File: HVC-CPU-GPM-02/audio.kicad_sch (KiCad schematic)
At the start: 0 parts

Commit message: Refactor schematic: * Move audio and video circuits to dedicated sheet * Move power and mechanical to dedicated sheet Modify P1 Cart Connector symbol to: * split out audio ports * organize pins for easier wiring Modify 74LS346 symbol: * Split A/B ports to allow moving functions to related circuits Modify X1 crystal footprint: * change from stock footprint to custom footprint Correct crystal name from Y1 to X1
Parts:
- added C34: 330p, Nintendo:C_Disc_D3.0mm_W2.0mm_P3.0mm, symbol Device:C
- added C35: 0.01u, Nintendo:C_Disc_D3.0mm_W2.0mm_P3.0mm, symbol Device:C
- added C7: 1u, Capacitor_THT:CP_Radial_D5.0mm_P2.50mm, symbol Device:C_Polarized
- added FC1: 39u, Inductor_THT:L_Axial_L5.0mm_D3.6mm_P10.00mm_Horizontal_Murata_BL01RN1A2A2, symbol Device:L_Ferrite
- added FC2: FerriteBead, Inductor_THT:L_Axial_L5.0mm_D3.6mm_P10.00mm_Horizontal_Murata_BL01RN1A2A2, symbol Device:FerriteBead
- added P1: CARTRIGE SLOT, Nintendo:Famicom_2x30_cartridge_connector, symbol Famicom:60p_cart_connector
- added Q1: 2SA937, Nintendo:PACKAGE_TRANSISTOR_FTR, symbol Simulation_SPICE:PNP
- added R1, R2: 100, Resistor_THT:R_Axial_DIN0207_L6.3mm_D2.5mm_P10.16mm_Horizontal, symbol Device:R
- added R3: 10k, Resistor_THT:R_Axial_DIN0207_L6.3mm_D2.5mm_P10.16mm_Horizontal, symbol Device:R
- added R4: 20k, Resistor_THT:R_Axial_DIN0207_L6.3mm_D2.5mm_P10.16mm_Horizontal, symbol Device:R
- added R5: 12, Resistor_THT:R_Axial_DIN0207_L6.3mm_D2.5mm_P10.16mm_Horizontal, symbol Device:R
- added R6: 150, Resistor_THT:R_Axial_DIN0207_L6.3mm_D2.5mm_P10.16mm_Horizontal, symbol Device:R
- added R7: 43k, Resistor_THT:R_Axial_DIN0207_L6.3mm_D2.5mm_P10.16mm_Horizontal, symbol Device:R
- added U7: 74LS368, Package_DIP:DIP-16_W7.62mm, symbol Famicom:74LS368
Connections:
- new net: C7.2, R3.2, R4.2, R5.2
- new net +5V: R6.1
- new net AUX_SND: C7.1, R7.1, U7.14 (IN2b)
- new net CPU_SND1: R2.1, R4.1
- new net CPU_SND2: R1.1, R5.1
- new net GND: C34.2, C35.2, Q1.1 (C), R1.2, R2.2, U7.15 (~{OEb})
- new net MIC: R3.1
- new net PA13: U7.12 (IN1b)
- new net PPU_VIDEO: Q1.2 (B)
- new net RF_AUDIO: C35.1, FC1.2
- new net RF_VIDEO: C34.1, FC2.2
- new net SOUND: P1.45 (SNDI), R7.2, U7.13 (~{OUT2b})
- new net SOUND+CART: FC1.1, P1.46 (SNDO)
- new net VID_A: FC2.1, Q1.3 (E), R6.2
- new net ~{PA13}: U7.11 (~{OUT1b})
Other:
- note added: "AUDIO MIXER"
- note added: "VIDEO AMP"

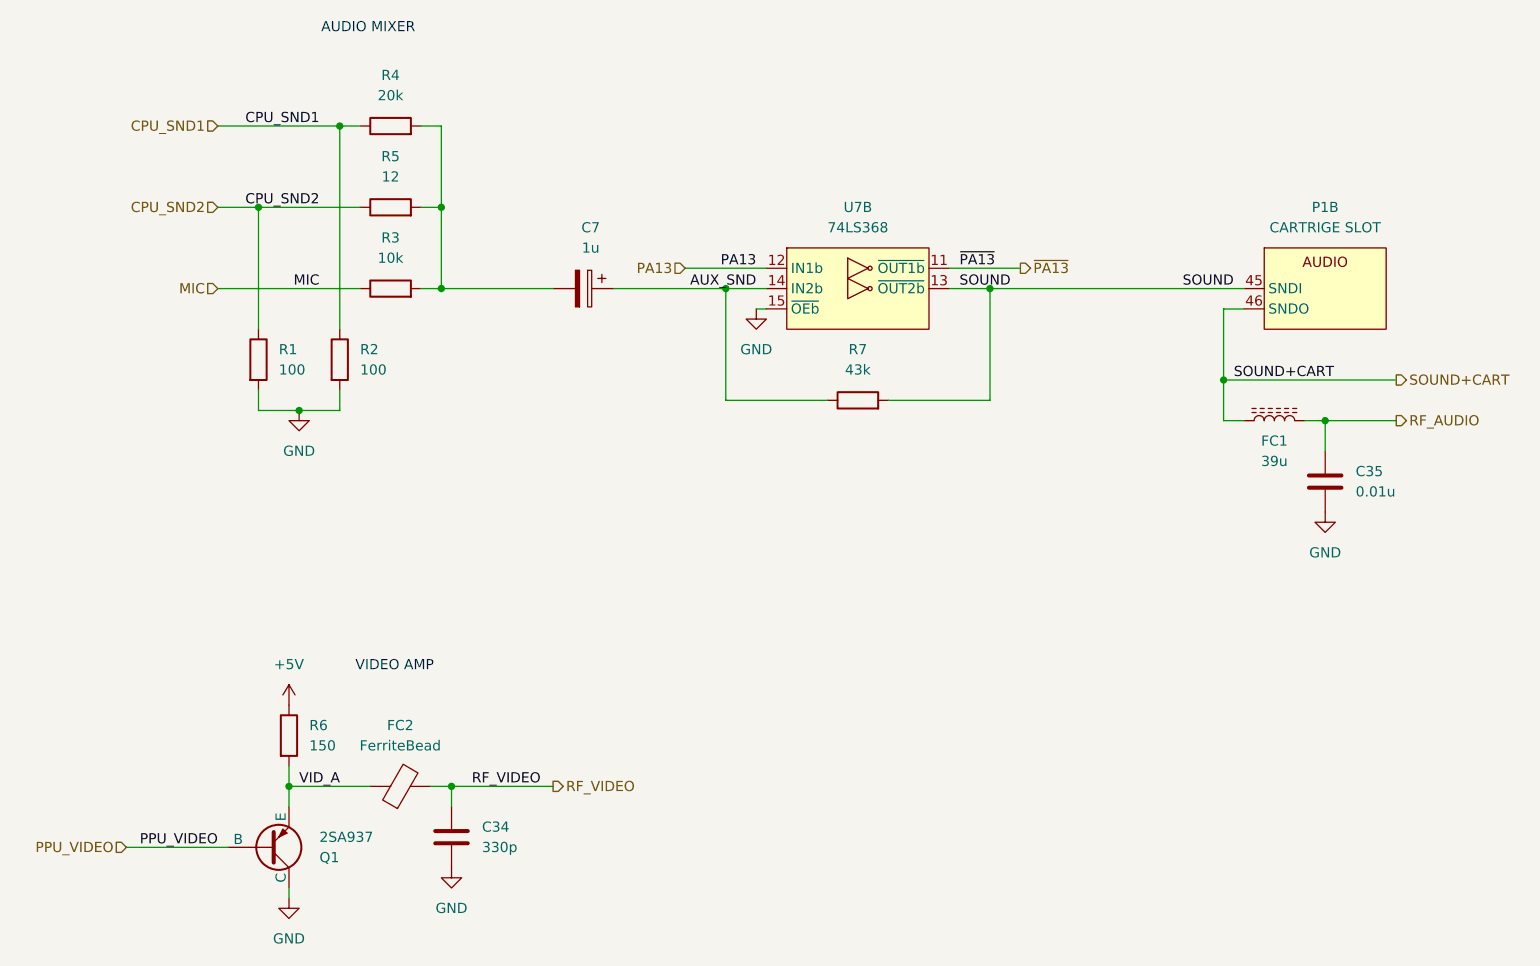
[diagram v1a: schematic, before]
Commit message: Change symbols to functional layout instead of pin map layout Add technical page to store pinouts Organize and compact root page
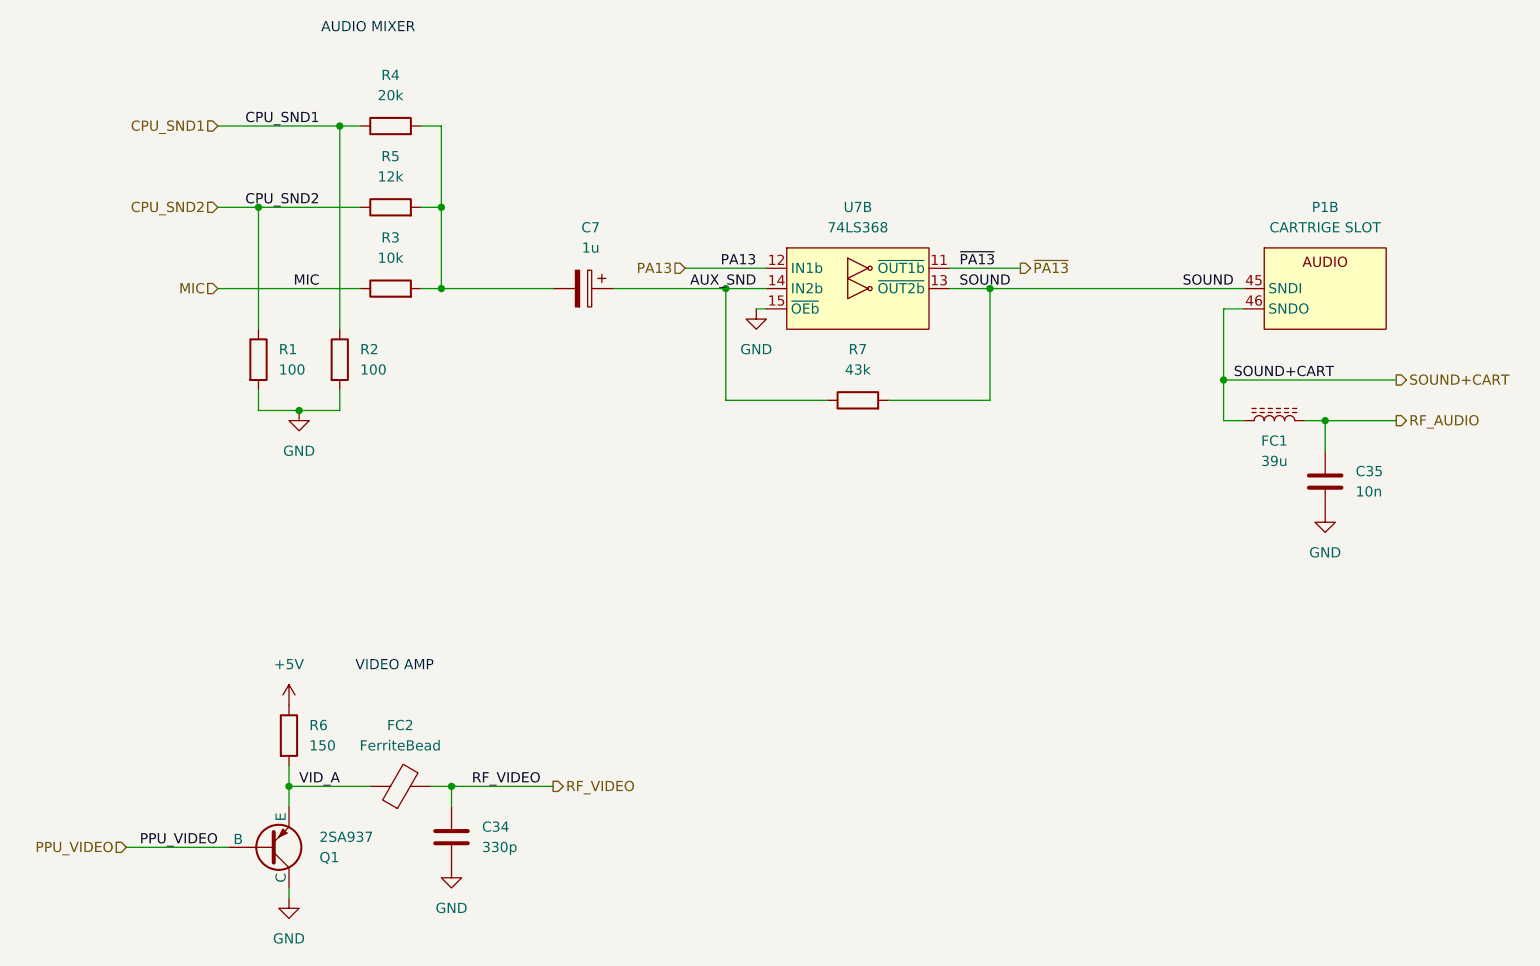
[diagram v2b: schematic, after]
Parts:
- C35: value 0.01u -> 10n
- R5: value 12 -> 12k
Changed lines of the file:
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@@
 			)
 		)
-		(property "Value" "12"
+		(property "Value" "12k"
 			(at 93.98 83.82 90)
 			(effects
@@
 			)
 		)
-		(property "Value" "0.01u"
+		(property "Value" "10n"
 			(at 214.63 123.1899 0)
 			(effects

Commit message: Rearranged pins on some symbols to simplify schematic wiring Removed schematics for controller PCBs Added PNG version of schematics
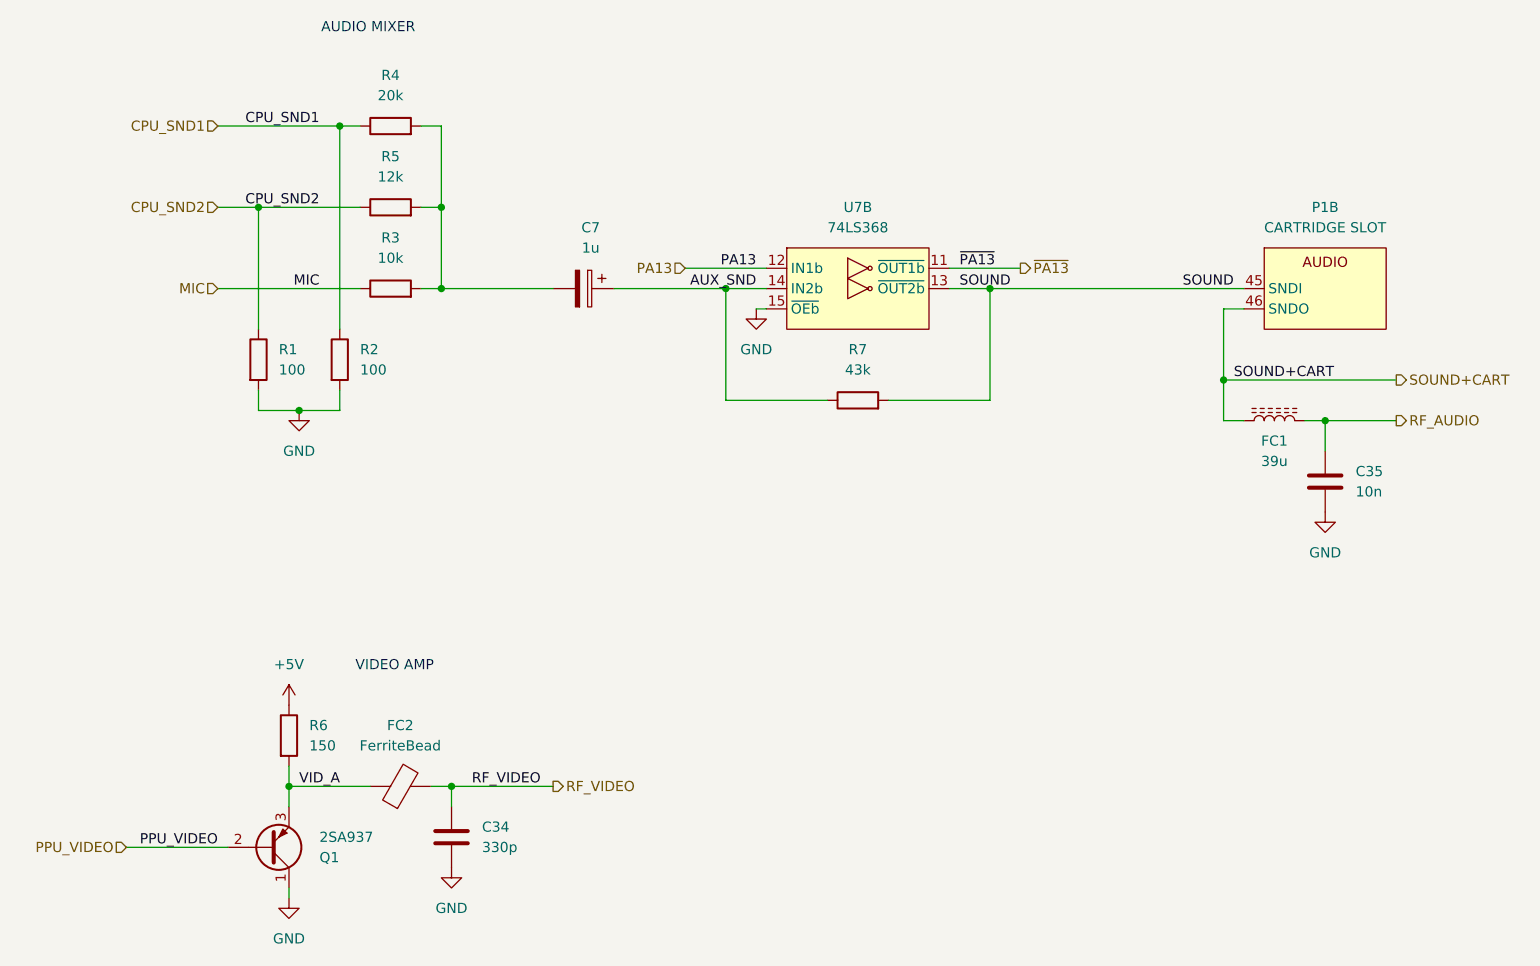
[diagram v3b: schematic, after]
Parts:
- P1: value CARTRIGE SLOT -> CARTRIDGE SLOT
- Q1: symbol Simulation_SPICE:PNP -> Transistor_BJT:Q_PNP_CBE
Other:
- title: (none) -> Nintendo Famicom Mainboard
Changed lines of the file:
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@@
 	(generator_version "9.0")
 	(paper "A4")
+	(title_block
+		(title "Nintendo Famicom Mainboard")
+		(date "2025-10-30")
+		(rev "1")
+	)
 	(text "AUDIO MIXER"
 		(exclude_from_sim no)
@@
 			)
 		)
-		(property "Value" "CARTRIGE SLOT"
+		(property "Value" "CARTRIDGE SLOT"
 			(at 210.82 90.17 0)
 			(effects
@@
 	)
 	(symbol
-		(lib_id "Simulation_SPICE:PNP")
+		(lib_id "Transistor_BJT:Q_PNP_CBE")
 		(at 78.74 167.64 0)
 		(mirror x)
@@
 		)
 		(property "Footprint" "Nintendo:PACKAGE_TRANSISTOR_FTR"
-			(at 114.3 167.64 0)
-			(effects
-				(font
-					(size 1.27 1.27)
-				)
-				(hide yes)
-			)
-		)
-		(property "Datasheet" "https://ngspice.sourceforge.io/docs/ngspice-html-manual/manual.xhtml#cha_BJTs"
-			(at 114.3 167.64 0)
-			(effects
-				(font
-					(size 1.27 1.27)
-				)
-				(hide yes)
-			)
-		)
-		(property "Description" "Bipolar transistor symbol for simulation only, substrate tied to the emitter"
+			(at 83.82 170.18 0)
+			(effects
+				(font
+					(size 1.27 1.27)
+				)
+				(hide yes)
+			)
+		)
+		(property "Datasheet" "~"
 			(at 78.74 167.64 0)
 			(effects
+				(font
+					(size 1.27 1.27)
+				)
+				(hide yes)
+			)
+		)
+		(property "Description" "PNP transistor, collector/base/emitter"
+			(at 78.74 167.64 0)
+			(effects

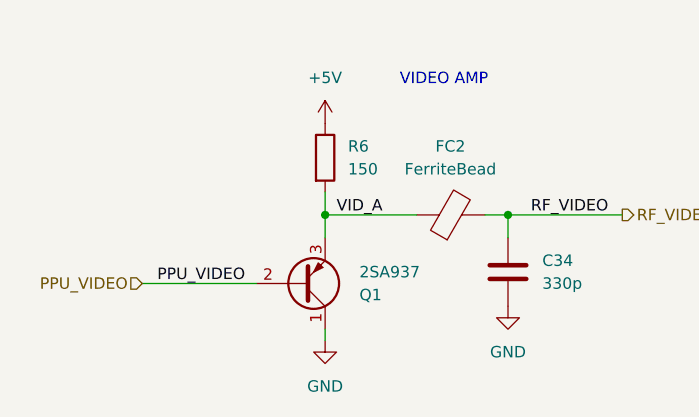
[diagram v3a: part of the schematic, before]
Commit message: annotate schematics, correct PCB/schematic parity issure, add datasheets
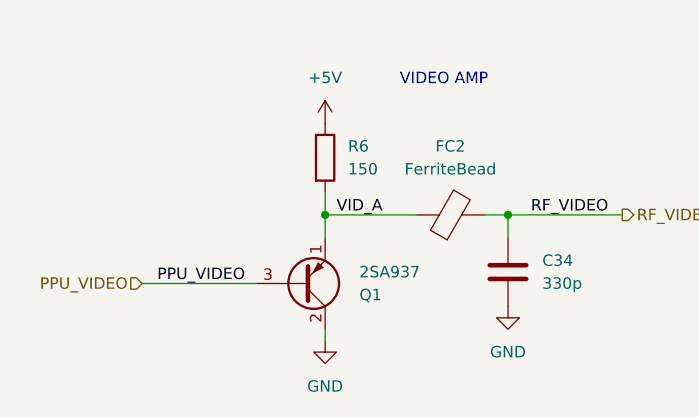
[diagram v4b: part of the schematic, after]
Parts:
- C34, C35: footprint Nintendo:C_Disc_D3.0mm_W2.0mm_P3.0mm -> Nintendo:C_Disc_NoSilk_D3.0mm_W2.0mm_P3.0mm
- C7: footprint Capacitor_THT:CP_Radial_D5.0mm_P2.50mm -> Nintendo:CP_Radial_D5.0mm_P2.50mm
- FC1, FC2: footprint Inductor_THT:L_Axial_L5.0mm_D3.6mm_P10.00mm_Horizontal_Murata_BL01RN1A2A2 -> Nintendo:L_Axial_NoSilk_L5.0mm_D3.6mm_P10.00mm_Horizontal_Murata_BL01RN1A2A2
- Q1: symbol Transistor_BJT:Q_PNP_CBE -> Transistor_BJT:Q_PNP_ECB
- R1, R2, R3, R4, R5, R6, R7: footprint Resistor_THT:R_Axial_DIN0207_L6.3mm_D2.5mm_P10.16mm_Horizontal -> Nintendo:R_Axial_NoSilk_DIN0207_L6.3mm_D2.5mm_P10.16mm_Horizontal
- U7: footprint Package_DIP:DIP-16_W7.62mm -> Nintendo:DIP-16_W7.62mm
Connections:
- net GND: now also Q1.2 (C); no longer Q1.1 (C)
- net PPU_VIDEO: now also Q1.3 (B); no longer Q1.2 (B)
- net VID_A: now also Q1.1 (E); no longer Q1.3 (E)
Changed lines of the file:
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@@
 			)
 		)
-		(property "Footprint" "Resistor_THT:R_Axial_DIN0207_L6.3mm_D2.5mm_P10.16mm_Horizontal"
+		(property "Footprint" "Nintendo:R_Axial_NoSilk_DIN0207_L6.3mm_D2.5mm_P10.16mm_Horizontal"
 			(at 79.502 153.67 90)
 			(effects
@@
 			)
 		)
-		(property "Footprint" "Resistor_THT:R_Axial_DIN0207_L6.3mm_D2.5mm_P10.16mm_Horizontal"
+		(property "Footprint" "Nintendo:R_Axial_NoSilk_DIN0207_L6.3mm_D2.5mm_P10.16mm_Horizontal"
 			(at 93.98 89.408 90)
 			(effects
@@
 			)
 		)
-		(property "Footprint" "Package_DIP:DIP-16_W7.62mm"
+		(property "Footprint" "Nintendo:DIP-16_W7.62mm"
 			(at 152.4 92.71 0)
 			(effects
@@
 			)
 		)
-		(property "Datasheet" "http://www.ti.com/lit/gpn/sn74LS368"
+		(property "Datasheet" "kicad-embed://74LS368.pdf"
 			(at 152.4 92.71 0)
 			(effects
@@
 			)
 		)
-		(property "Footprint" "Resistor_THT:R_Axial_DIN0207_L6.3mm_D2.5mm_P10.16mm_Horizontal"
+		(property "Footprint" "Nintendo:R_Axial_NoSilk_DIN0207_L6.3mm_D2.5mm_P10.16mm_Horizontal"
 			(at 75.692 106.68 90)
 			(effects
@@
 			)
 		)
-		(property "Footprint" "Resistor_THT:R_Axial_DIN0207_L6.3mm_D2.5mm_P10.16mm_Horizontal"
+		(property "Footprint" "Nintendo:R_Axial_NoSilk_DIN0207_L6.3mm_D2.5mm_P10.16mm_Horizontal"
 			(at 152.4 113.538 90)
 			(effects
@@
 			)
 		)
-		(property "Footprint" "Resistor_THT:R_Axial_DIN0207_L6.3mm_D2.5mm_P10.16mm_Horizontal"
+		(property "Footprint" "Nintendo:R_Axial_NoSilk_DIN0207_L6.3mm_D2.5mm_P10.16mm_Horizontal"
 			(at 85.852 106.68 90)
 			(effects
@@
 			)
 		)
-		(property "Footprint" "Inductor_THT:L_Axial_L5.0mm_D3.6mm_P10.00mm_Horizontal_Murata_BL01RN1A2A2"
+		(property "Footprint" "Nintendo:L_Axial_NoSilk_L5.0mm_D3.6mm_P10.00mm_Horizontal_Murata_BL01RN1A2A2"
 			(at 95.25 161.798 90)
 			(effects
@@
 			)
 		)
-		(property "Footprint" "Capacitor_THT:CP_Radial_D5.0mm_P2.50mm"
+		(property "Footprint" "Nintendo:CP_Radial_D5.0mm_P2.50mm"
 			(at 114.3 98.7552 0)
 			(effects
@@
 			)
 		)
-		(property "Footprint" "Resistor_THT:R_Axial_DIN0207_L6.3mm_D2.5mm_P10.16mm_Horizontal"
+		(property "Footprint" "Nintendo:R_Axial_NoSilk_DIN0207_L6.3mm_D2.5mm_P10.16mm_Horizontal"
 			(at 93.98 99.568 90)
 			(effects
@@
 			)
 		)
-		(property "Footprint" "Resistor_THT:R_Axial_DIN0207_L6.3mm_D2.5mm_P10.16mm_Horizontal"
+		(property "Footprint" "Nintendo:R_Axial_NoSilk_DIN0207_L6.3mm_D2.5mm_P10.16mm_Horizontal"
 			(at 93.98 79.248 90)
 			(effects
@@
 			)
 		)
-		(property "Footprint" "Nintendo:C_Disc_D3.0mm_W2.0mm_P3.0mm"
+		(property "Footprint" "Nintendo:C_Disc_NoSilk_D3.0mm_W2.0mm_P3.0mm"
 			(at 211.7852 125.73 0)
 			(effects
@@
 			)
 		)
-		(property "Footprint" "Inductor_THT:L_Axial_L5.0mm_D3.6mm_P10.00mm_Horizontal_Murata_BL01RN1A2A2"
+		(property "Footprint" "Nintendo:L_Axial_NoSilk_L5.0mm_D3.6mm_P10.00mm_Horizontal_Murata_BL01RN1A2A2"
 			(at 204.47 114.3 0)
 			(effects
@@
 			)
 		)
-		(property "Footprint" "Nintendo:C_Disc_D3.0mm_W2.0mm_P3.0mm"
+		(property "Footprint" "Nintendo:C_Disc_NoSilk_D3.0mm_W2.0mm_P3.0mm"
 			(at 102.5652 170.18 0)
 			(effects
@@
 	)
 	(symbol
-		(lib_id "Transistor_BJT:Q_PNP_CBE")
+		(lib_id "Transistor_BJT:Q_PNP_ECB")
 		(at 78.74 167.64 0)
 		(mirror x)
@@
 			)
 		)
-		(property "Datasheet" "~"
+		(property "Datasheet" "kicad-embed://2SA937.PDF"
 			(at 78.74 167.64 0)
 			(effects
@@
 			)
 		)
-		(property "Description" "PNP transistor, collector/base/emitter"
+		(property "Description" "PNP transistor, emitter/collector/base"
 			(at 78.74 167.64 0)
 			(effects
